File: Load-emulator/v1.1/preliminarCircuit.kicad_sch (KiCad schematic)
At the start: 2 parts, among them J6 532610471, J9 533980871

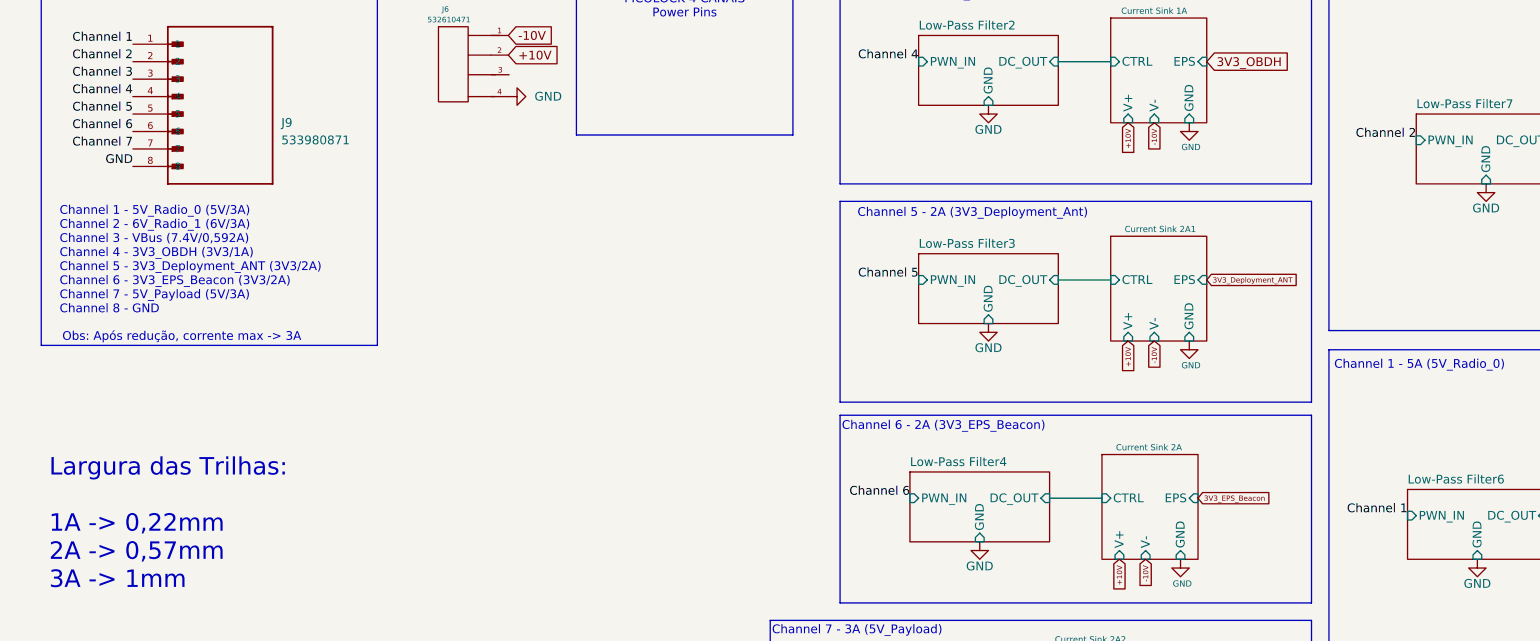
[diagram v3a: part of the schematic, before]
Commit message: Todas trilhas necessárias refeitas. Alterado posição do primeiro e segundo canal. Zero erros.
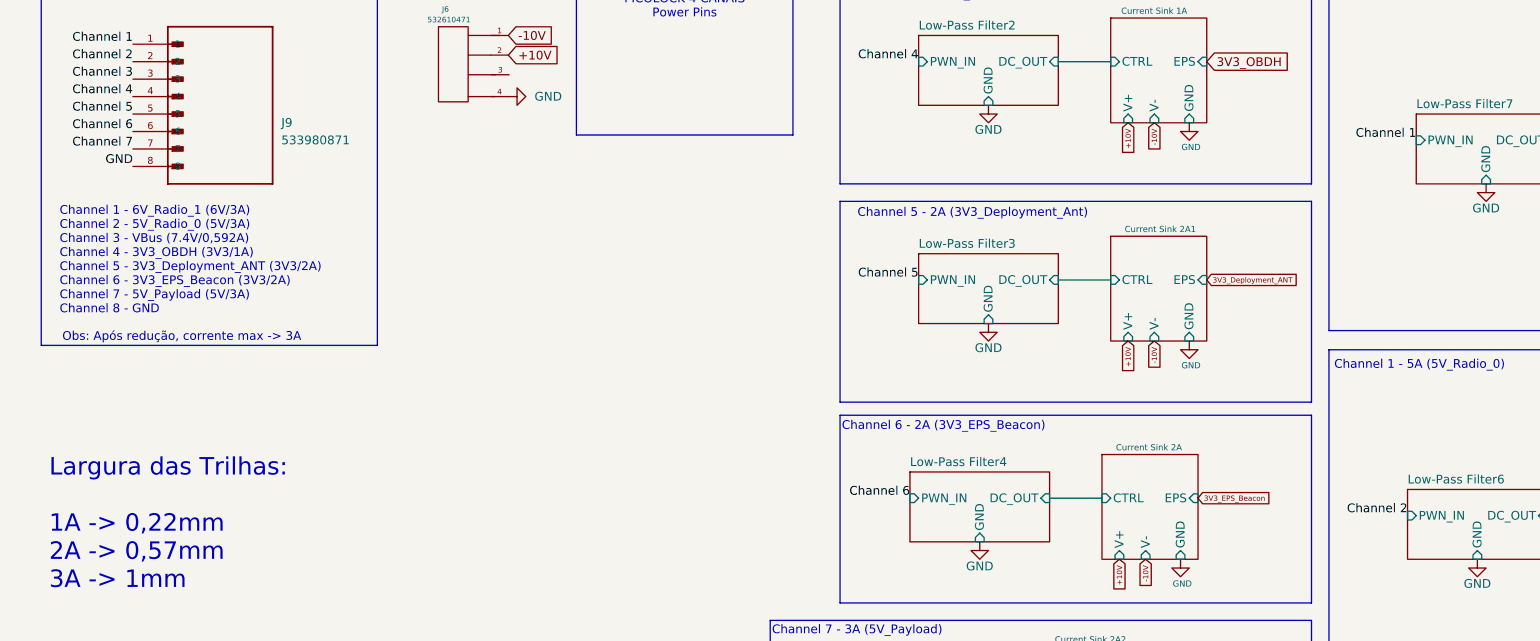
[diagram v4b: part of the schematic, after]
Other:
- note added: "Channel 1 - 6V_Radio_1 (6V/3A) Channel 2 - 5V_Radio_0 (5V/3A) Channel 3 - VBus (7.4V/0,592A) Channel 4 - 3V3_OBDH (3V3/1A) Channel 5 - 3V3_Deployment_ANT (3V3/2A) Channel 6 - 3V3_EPS_Beacon (3V3/2A) Channel 7 - 5V_Payload (5V/3A) Channel 8 - GND"
- note removed: "Channel 1 - 5V_Radio_0 (5V/3A) Channel 2 - 6V_Radio_1 (6V/3A) Channel 3 - VBus (7.4V/0,592A) Channel 4 - 3V3_OBDH (3V3/1A) Channel 5 - 3V3_Deployment_ANT (3V3/2A) Channel 6 - 3V3_EPS_Beacon (3V3/2A) Channel 7 - 5V_Payload (5V/3A) Channel 8 - GND"
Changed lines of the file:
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@@
 		)
 	)
-	(text "Channel 1 - 5V_Radio_0 (5V/3A)\nChannel 2 - 6V_Radio_1 (6V/3A)\nChannel 3 - VBus (7.4V/0,592A)\nChannel 4 - 3V3_OBDH (3V3/1A)\nChannel 5 - 3V3_Deployment_ANT (3V3/2A)\nChannel 6 - 3V3_EPS_Beacon (3V3/2A)\nChannel 7 - 5V_Payload (5V/3A)\nChannel 8 - GND"
+	(text "Channel 1 - 6V_Radio_1 (6V/3A)\nChannel 2 - 5V_Radio_0 (5V/3A)\nChannel 3 - VBus (7.4V/0,592A)\nChannel 4 - 3V3_OBDH (3V3/1A)\nChannel 5 - 3V3_Deployment_ANT (3V3/2A)\nChannel 6 - 3V3_EPS_Beacon (3V3/2A)\nChannel 7 - 5V_Payload (5V/3A)\nChannel 8 - GND"
 		(exclude_from_sim no)
 		(at 17.272 56.896 0)
@@
 		)
 	)
-	(label "Channel 2"
+	(label "Channel 1"
 		(at 214.63 39.37 180)
 		(effects
@@
 		)
 	)
-	(label "Channel 1"
+	(label "Channel 2"
 		(at 213.36 93.98 180)
 		(effects
